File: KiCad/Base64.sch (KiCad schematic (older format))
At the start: 24 parts, among them J1 1473149-4, J2 Conn_01x03, U1 501MLFT, U10 68000_PinHeader, U2 SN74CBTD3861DGVR, U3 SN74CBTD3861DGVR, U4 SN74CBTD3861DGVR, U5 SN74CBTD3861DGVR, U6 SN74CBTD3861DGVR, U7 SN74CBTD3861DGVR, U8 SN74CBTD3861DGVR, U9 74AHCT1G17

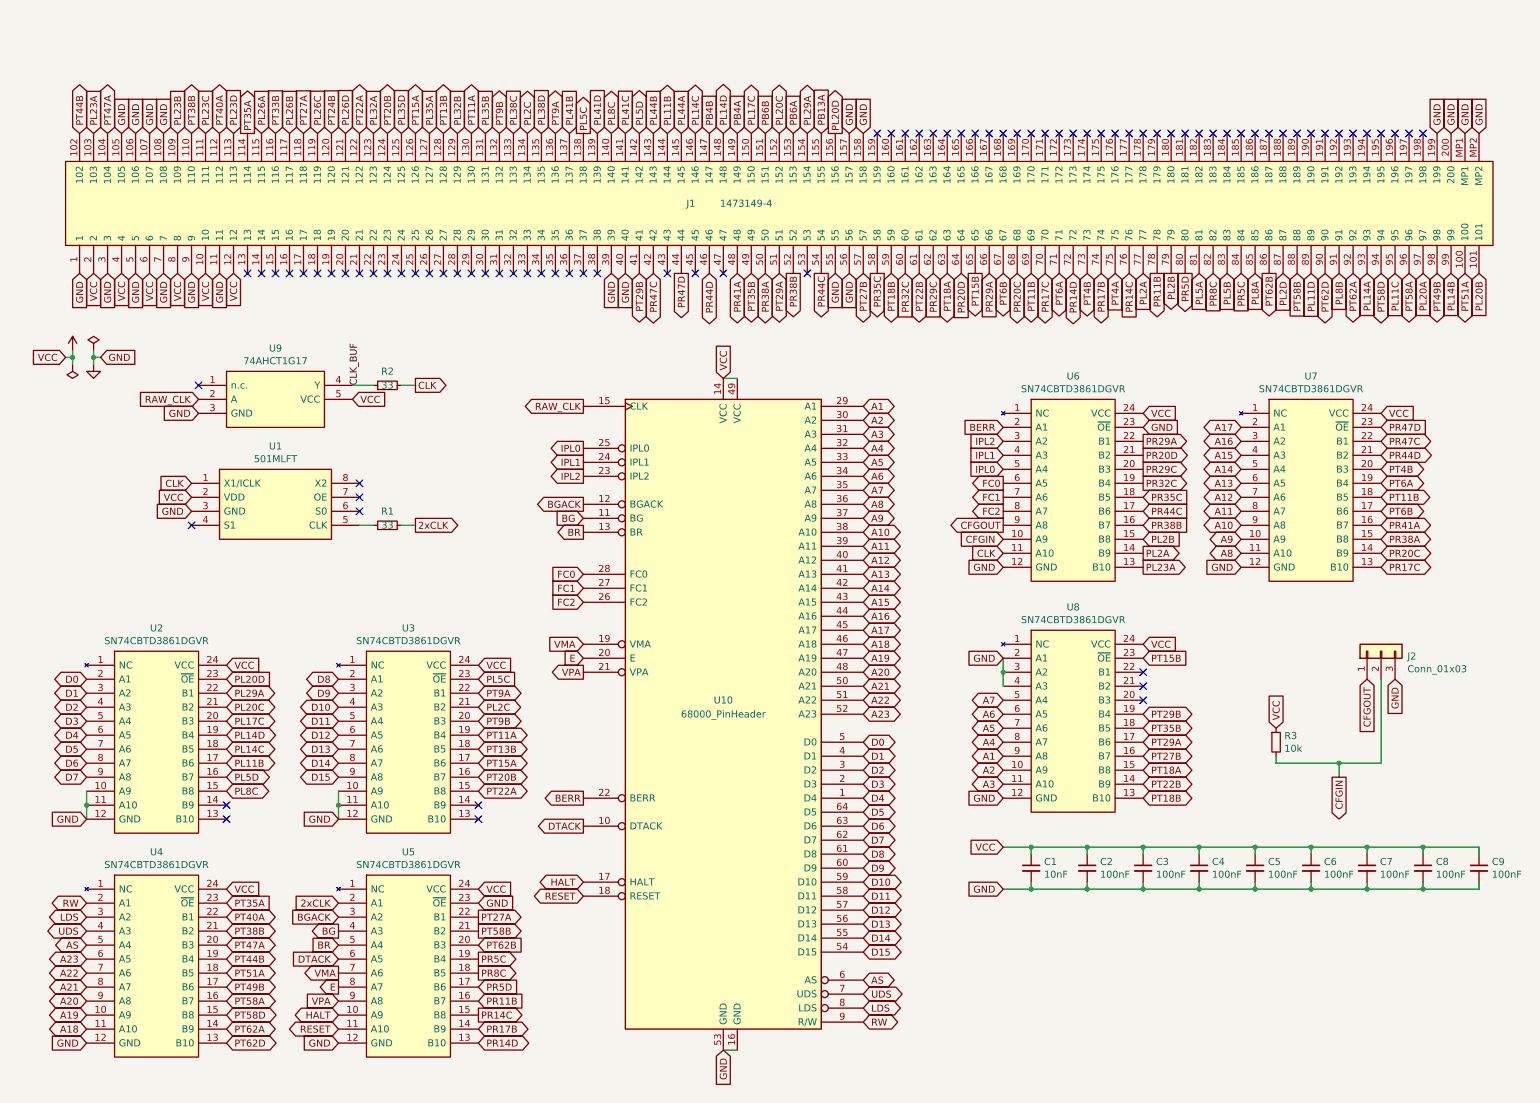
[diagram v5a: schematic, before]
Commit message: Redesign with 570BLFT in order to generate a phase aligned 84 MHz clock
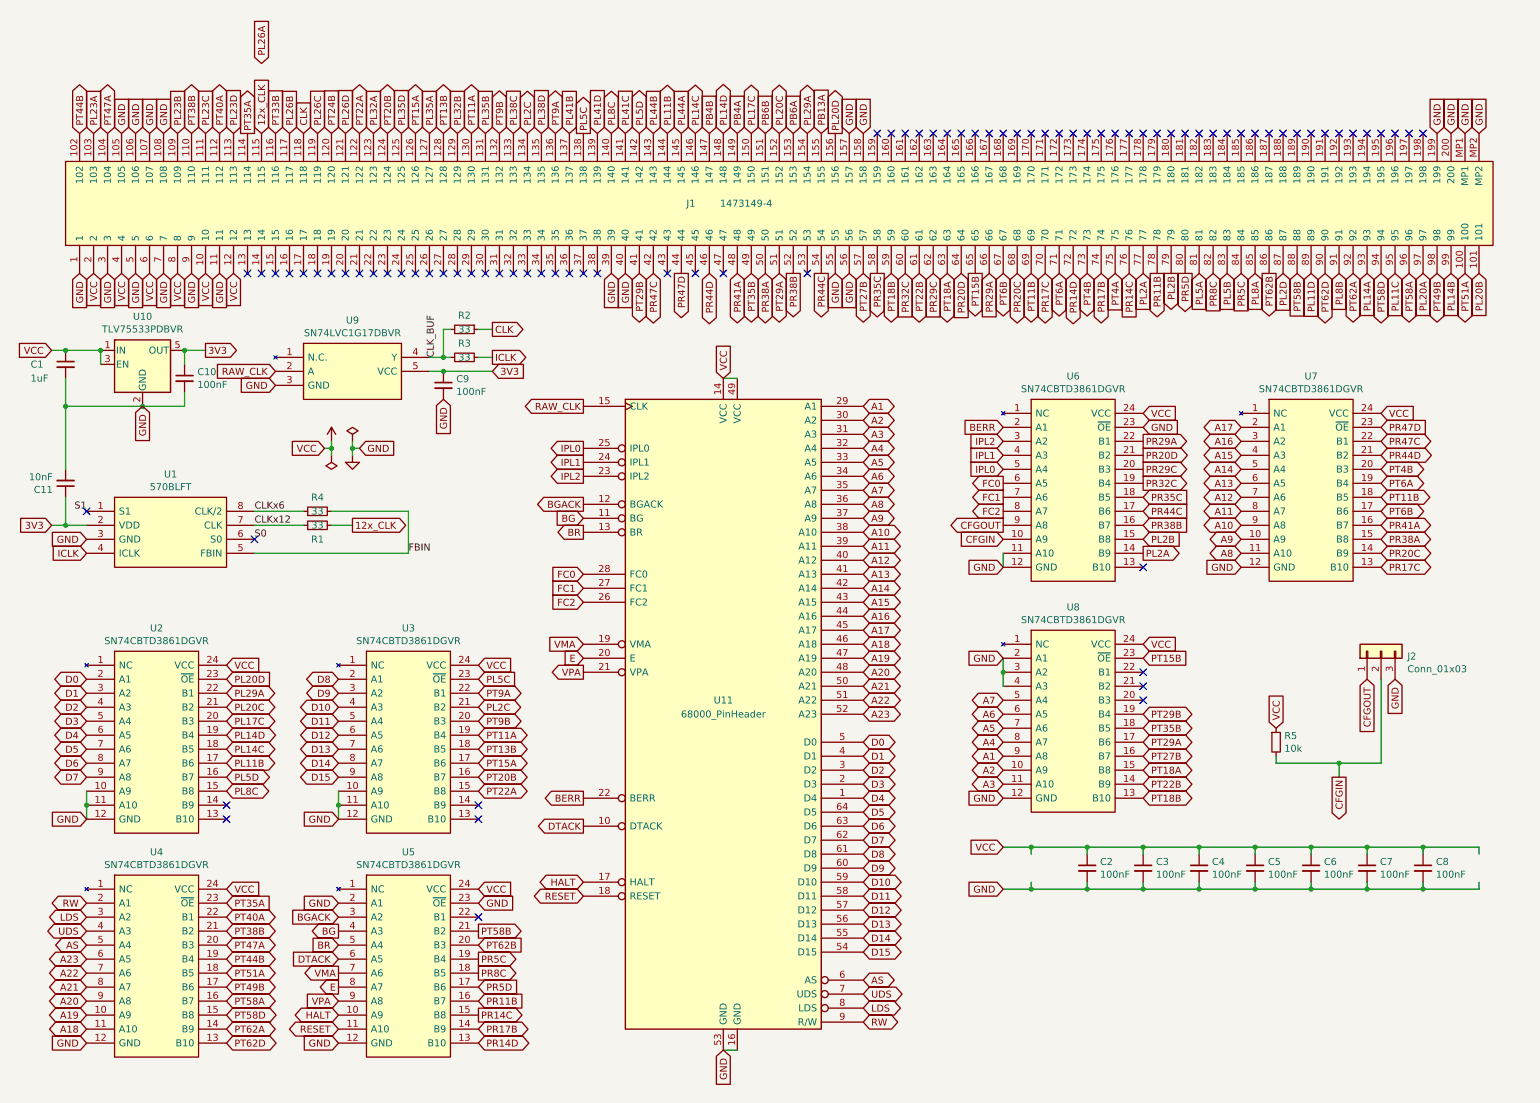
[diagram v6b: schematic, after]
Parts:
- removed U1: 501MLFT, Package_SO:SOIC-8_3.9x4.9mm_P1.27mm, symbol Base64:501MLFT
- removed U9: 74AHCT1G17, Base64:SOT95P275X110-5N, symbol Base64:74AHCT1G17
- added C1: 1uF, Capacitor_SMD:C_0805_2012Metric, symbol Device:C_Small
- added C10: 100nF, Capacitor_SMD:C_0603_1608Metric, symbol Device:C_Small
- added R2: 33, Resistor_SMD:R_0805_2012Metric, symbol Device:R_Small
- added R4: 33, Resistor_SMD:R_0603_1608Metric, symbol Device:R_Small
- added U1: 570BLFT, Package_SO:SOIC-8_3.9x4.9mm_P1.27mm, symbol Base64:570BLFT
- added U10: TLV75533PDBVR, Package_TO_SOT_SMD:SOT-23-5, symbol Regulator_Linear:TLV73312PDBV
- added U9: SN74LVC1G17DBVR, Base64:SOT95P280X145-5N, symbol Base64:SN74LVC1G17DBVR
- R1: footprint Resistor_SMD:R_0603_1608Metric -> Resistor_SMD:R_0805_2012Metric
- renumbered C1 to C11, R2 to R3, R3 to R5, U10 to U11
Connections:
- net labels added: 12x_CLK, 3V3, CLKx12, CLKx6, FBIN, ICLK, S0, S1
- net labels removed: 2xCLK, PT27A
- wire segments 59 -> 83
- no-connect marks 82 -> 81
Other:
- moved on the sheet: C11, C9, R1, R3

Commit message: Add text notes for CLK lines
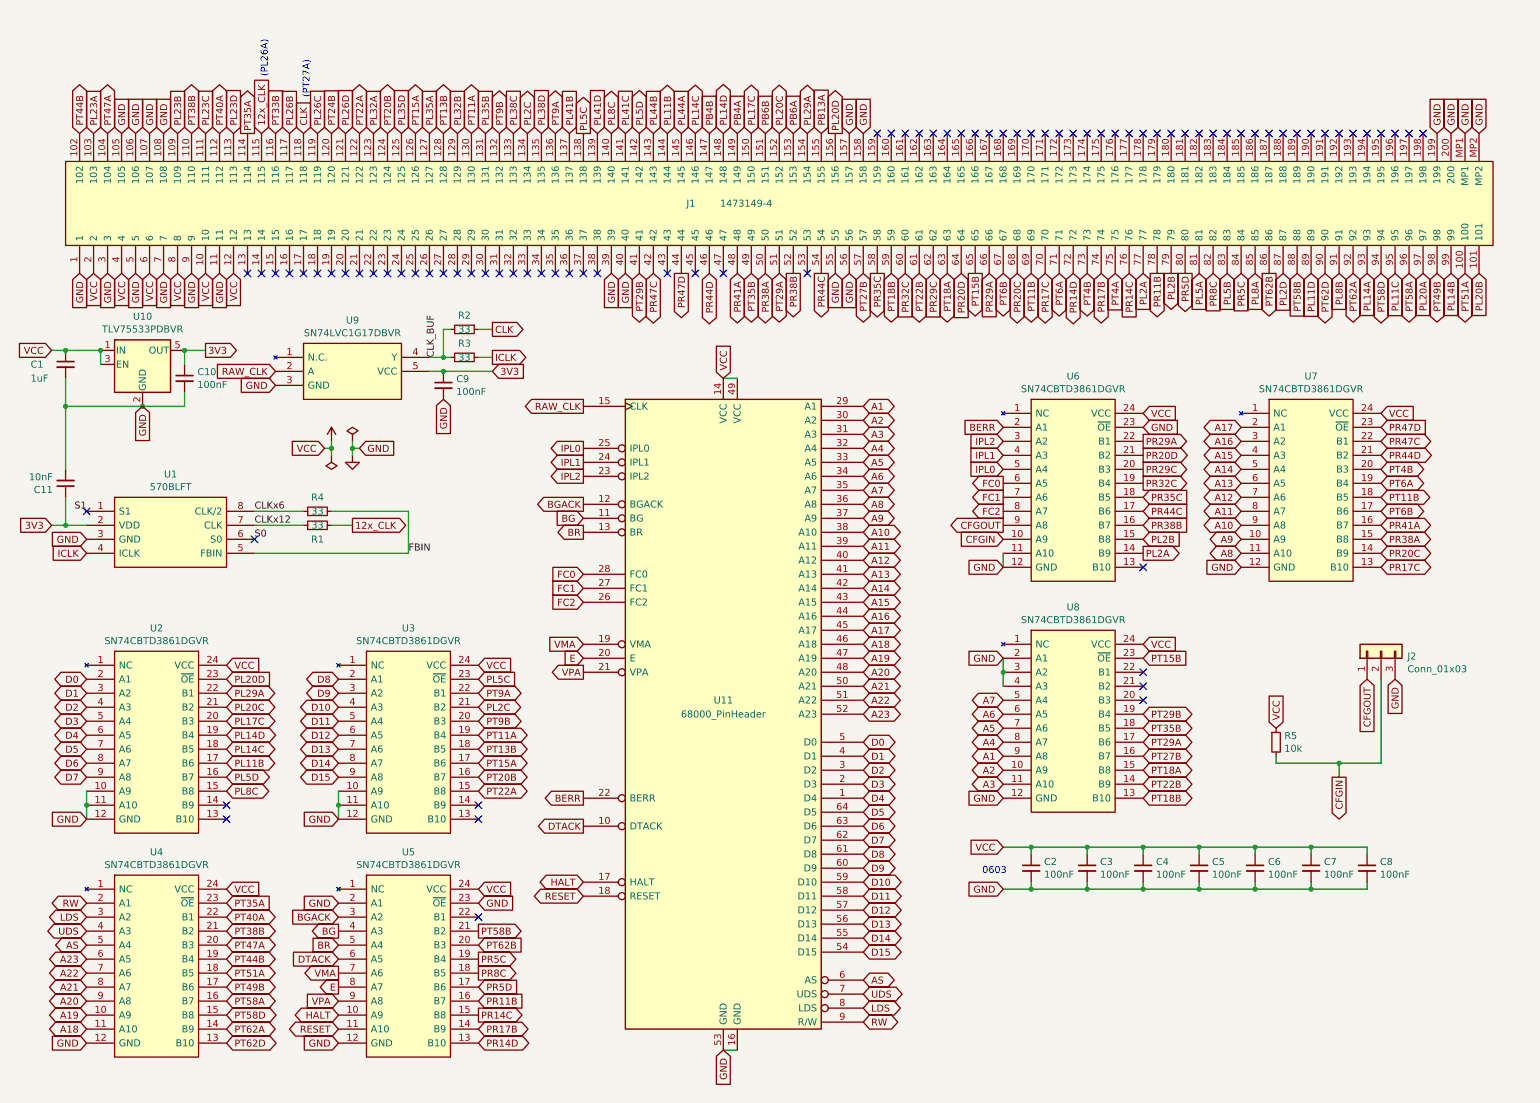
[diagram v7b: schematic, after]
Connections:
- net labels removed: PL26A
- wire segments 83 -> 75
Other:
- note added: "(PL26A)"
- note added: "(PT27A)"
- note added: "0603"
- moved on the sheet: C2, C3, C4, C5, C6, C7, C8
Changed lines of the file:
@@
 Text GLabel 2100 950  1    50   Output ~ 0
 PT35A
-Text GLabel 2200 450  1    50   Input ~ 0
-PL26A
 Text GLabel 2300 950  1    50   Input ~ 0
 PT33B
@@
 L Device:C_Small C2
 U 1 1 69070834
+P 7700 6200
+F 0 "C2" H 7792 6246 50  0000 L CNN
+F 1 "100nF" H 7792 6155 50  0000 L CNN
+F 2 "Capacitor_SMD:C_0603_1608Metric" H 7700 6200 50  0001 C CNN
+F 3 "~" H 7700 6200 50  0001 C CNN
+	1    7700 6200
+	1    0    0    -1
+$EndComp
+Text GLabel 7500 6050 0    50   Input ~ 0
+VCC
+Text GLabel 7500 6350 0    50   Input ~ 0
+GND
+Wire Wire Line
+	8100 6050 8100 6100
+Wire Wire Line
+	8100 6350 8100 6300
+$Comp
+L Device:C_Small C3
+U 1 1 690AB253
 P 8100 6200
-F 0 "C2" H 8192 6246 50  0000 L CNN
+F 0 "C3" H 8192 6246 50  0000 L CNN
 F 1 "100nF" H 8192 6155 50  0000 L CNN
 F 2 "Capacitor_SMD:C_0603_1608Metric" H 8100 6200 50  0001 C CNN
@@
 	1    0    0    -1
 $EndComp
-Text GLabel 7500 6050 0    50   Input ~ 0
-VCC
-Text GLabel 7500 6350 0    50   Input ~ 0
-GND
-Wire Wire Line
-	8100 6050 8100 6100
-Wire Wire Line
-	8100 6350 8100 6300
-$Comp
-L Device:C_Small C3
-U 1 1 690AB253
-P 8500 6200
-F 0 "C3" H 8592 6246 50  0000 L CNN
-F 1 "100nF" H 8592 6155 50  0000 L CNN
-F 2 "Capacitor_SMD:C_0603_1608Metric" H 8500 6200 50  0001 C CNN
-F 3 "~" H 8500 6200 50  0001 C CNN
-	1    8500 6200
-	1    0    0    -1
-$EndComp
 Wire Wire Line
 	8500 6050 8500 6100
 Wire Wire Line
 	8500 6350 8500 6300
-Wire Wire Line
-	7500 6050 7700 6050
 Wire Wire Line
 	7500 6350 7700 6350
@@
 $EndComp
 Wire Wire Line
-	7700 6100 7700 6050
-Connection ~ 7700 6050
-Wire Wire Line
-	7700 6050 8100 6050
-Wire Wire Line
 	7700 6300 7700 6350
 Connection ~ 7700 6350
@@
 L Device:C_Small C4
 U 1 1 69111C18
+P 8500 6200
+F 0 "C4" H 8592 6246 50  0000 L CNN
+F 1 "100nF" H 8592 6155 50  0000 L CNN
+F 2 "Capacitor_SMD:C_0603_1608Metric" H 8500 6200 50  0001 C CNN
+F 3 "~" H 8500 6200 50  0001 C CNN
+	1    8500 6200
+	1    0    0    -1
+$EndComp
+Wire Wire Line
+	8900 6100 8900 6050
+Wire Wire Line
+	8900 6050 8500 6050
+Connection ~ 8500 6050
+Wire Wire Line
+	8900 6300 8900 6350
+Wire Wire Line
+	8900 6350 8500 6350
+Connection ~ 8500 6350
+$Comp
+L Device:C_Small C5
+U 1 1 69116650
 P 8900 6200
-F 0 "C4" H 8992 6246 50  0000 L CNN
+F 0 "C5" H 8992 6246 50  0000 L CNN
 F 1 "100nF" H 8992 6155 50  0000 L CNN
 F 2 "Capacitor_SMD:C_0603_1608Metric" H 8900 6200 50  0001 C CNN
@@
 $EndComp
 Wire Wire Line
-	8900 6100 8900 6050
-Wire Wire Line
-	8900 6050 8500 6050
-Connection ~ 8500 6050
-Wire Wire Line
-	8900 6300 8900 6350
-Wire Wire Line
-	8900 6350 8500 6350
-Connection ~ 8500 6350
-$Comp
-L Device:C_Small C5
-U 1 1 69116650
+	9300 6100 9300 6050
+Wire Wire Line
+	9300 6050 8900 6050
+Connection ~ 8900 6050
+Wire Wire Line
+	8900 6350 9300 6350
+Wire Wire Line
+	9300 6350 9300 6300
+Connection ~ 8900 6350
+$Comp
+L Device:C_Small C6
+U 1 1 6914ABBB
 P 9300 6200
-F 0 "C5" H 9392 6246 50  0000 L CNN
+F 0 "C6" H 9392 6246 50  0000 L CNN
 F 1 "100nF" H 9392 6155 50  0000 L CNN
 F 2 "Capacitor_SMD:C_0603_1608Metric" H 9300 6200 50  0001 C CNN
@@
 $EndComp
 Wire Wire Line
-	9300 6100 9300 6050
-Wire Wire Line
-	9300 6050 8900 6050
-Connection ~ 8900 6050
-Wire Wire Line
-	8900 6350 9300 6350
-Wire Wire Line
-	9300 6350 9300 6300
-Connection ~ 8900 6350
-$Comp
-L Device:C_Small C6
-U 1 1 6914ABBB
+	9700 6100 9700 6050
+Wire Wire Line
+	9700 6050 9300 6050
+Connection ~ 9300 6050
+Wire Wire Line
+	9300 6350 9700 6350
+Wire Wire Line
+	9700 6350 9700 6300
+Connection ~ 9300 6350
+$Comp
+L Device:C_Small C7
+U 1 1 6916FCAA
 P 9700 6200
-F 0 "C6" H 9792 6246 50  0000 L CNN
+F 0 "C7" H 9792 6246 50  0000 L CNN
 F 1 "100nF" H 9792 6155 50  0000 L CNN
 F 2 "Capacitor_SMD:C_0603_1608Metric" H 9700 6200 50  0001 C CNN
@@
 $EndComp
 Wire Wire Line
-	9700 6100 9700 6050
-Wire Wire Line
-	9700 6050 9300 6050
-Connection ~ 9300 6050
-Wire Wire Line
-	9300 6350 9700 6350
-Wire Wire Line
-	9700 6350 9700 6300
-Connection ~ 9300 6350
-$Comp
-L Device:C_Small C7
-U 1 1 6916FCAA
+	9700 6350 10100 6350
+Wire Wire Line
+	10100 6350 10100 6300
+Connection ~ 9700 6350
+Wire Wire Line
+	10100 6100 10100 6050
+Wire Wire Line
+	10100 6050 9700 6050
+Connection ~ 9700 6050
+$Comp
+L Device:C_Small C8
+U 1 1 691BF310
 P 10100 6200
-F 0 "C7" H 10192 6246 50  0000 L CNN
+F 0 "C8" H 10192 6246 50  0000 L CNN
 F 1 "100nF" H 10192 6155 50  0000 L CNN
 F 2 "Capacitor_SMD:C_0603_1608Metric" H 10100 6200 50  0001 C CNN
@@
 	1    0    0    -1
 $EndComp
-Wire Wire Line
-	9700 6350 10100 6350
-Wire Wire Line
-	10100 6350 10100 6300
-Connection ~ 9700 6350
-Wire Wire Line
-	10100 6100 10100 6050
-Wire Wire Line
-	10100 6050 9700 6050
-Connection ~ 9700 6050
-$Comp
-L Device:C_Small C8
-U 1 1 691BF310
-P 10500 6200
-F 0 "C8" H 10592 6246 50  0000 L CNN
-F 1 "100nF" H 10592 6155 50  0000 L CNN
-F 2 "Capacitor_SMD:C_0603_1608Metric" H 10500 6200 50  0001 C CNN
-F 3 "~" H 10500 6200 50  0001 C CNN
-	1    10500 6200
-	1    0    0    -1
-$EndComp
-Wire Wire Line
-	10100 6050 10500 6050
-Wire Wire Line
-	10500 6050 10500 6100
-Connection ~ 10100 6050
-Wire Wire Line
-	10100 6350 10500 6350
-Wire Wire Line
-	10500 6350 10500 6300
-Connection ~ 10100 6350
 $Comp
 L Device:R_Small R5
@@
 	1    0    0    -1
 $EndComp
-Wire Wire Line
-	10900 6100 10900 6050
-Wire Wire Line
-	10900 6050 10500 6050
-Connection ~ 10500 6050
-Wire Wire Line
-	10900 6300 10900 6350
-Wire Wire Line
-	10900 6350 10500 6350
-Connection ~ 10500 6350
 $Comp
 L Base64:570BLFT U1
@@
 	1650 2900 1350 2900
 Connection ~ 1350 2900
+Text Notes 2250 550  1    50   ~ 0
+(PL26A)
+Text Notes 2550 700  1    50   ~ 0
+(PT27A)
+Wire Wire Line
+	7700 6050 8100 6050
+Wire Wire Line
+	7500 6050 7700 6050
+Connection ~ 7700 6050
+Wire Wire Line
+	7700 6100 7700 6050
+Text Notes 7350 6250 0    50   ~ 0
+0603
 $EndSCHEMATC
